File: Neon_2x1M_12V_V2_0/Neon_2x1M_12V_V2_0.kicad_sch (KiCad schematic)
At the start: 38 parts, among them J1 Conn_01x16_Pin, J2 Barrel_Jack_MountingPin, J3 Conn_01x16_Pin, J4 Barrel_Jack_MountingPin, J5 Barrel_Jack_MountingPin, J6 Conn_01x03_Pin, Q1 IRLML2502TRPBF, Q2 IRLML2502TRPBF, SW1 SW_Push, SW2 SW_Push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

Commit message: updated schematic and layout for V2.0
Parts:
- added J7, J8: Screw_Terminal_01x02, Connector_JST:JST_NV_B02P-NV_1x02_P5.00mm_Vertical, symbol Connector:Screw_Terminal_01x02
- J4, J5: now not fitted; now left out of the parts list
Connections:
- net +12V: now also J7.2 (Pin_2), J8.2 (Pin_2)
- net B_Jack: now also J8.1 (Pin_1); no longer J4.2
- net P_Jack: now also J4.2, J7.1 (Pin_1)
- net BUCK_SW: now reaches D2.1 (K), L1.1, U3.2 (OUT)

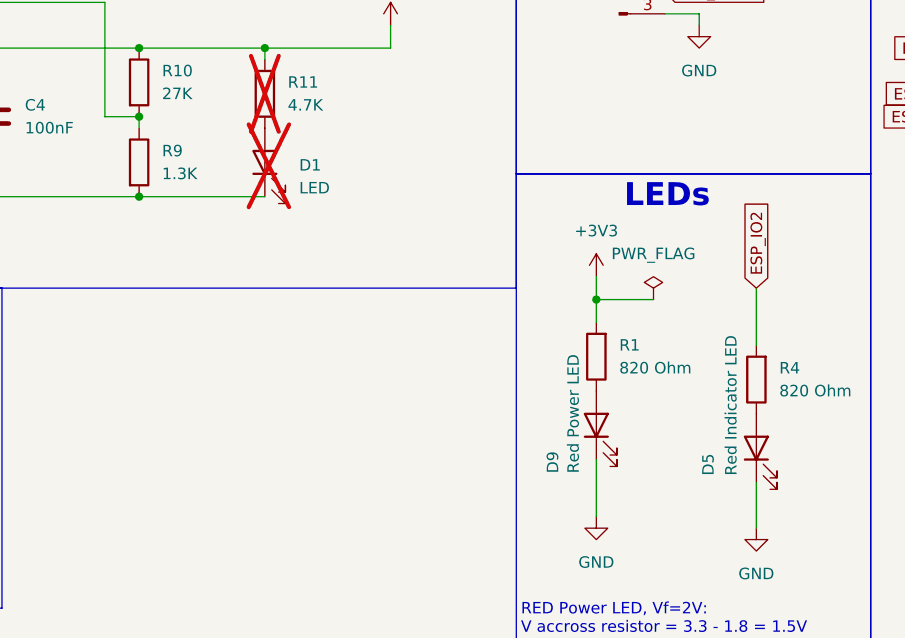
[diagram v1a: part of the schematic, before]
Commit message: updated BOM and generated BOM csv file also updated schematic and layout along
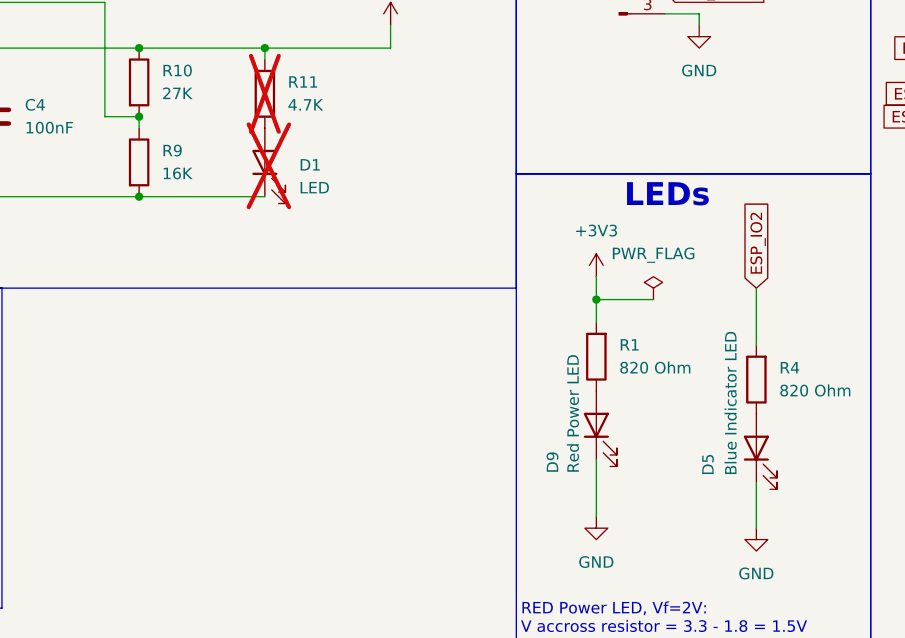
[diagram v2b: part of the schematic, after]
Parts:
- D5: value Red Indicator LED -> Blue Indicator LED
- R3, R6, R7, R8: footprint Resistor_SMD:R_0805_2012Metric_Pad1.20x1.40mm_HandSolder -> Resistor_SMD:R_1210_3225Metric_Pad1.30x2.65mm_HandSolder; link https://uge-one.com/product/0805-smd-chip-resistor-10k/?srs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 -> https://makerselectronics.com/product/chip-resistor-smd-10k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
- R9: value 1.3K -> 16K
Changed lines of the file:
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@@
 			)
 		)
-		(property "Footprint" "Resistor_SMD:R_0805_2012Metric_Pad1.20x1.40mm_HandSolder"
+		(property "Footprint" "Resistor_SMD:R_1210_3225Metric_Pad1.30x2.65mm_HandSolder"
 			(at 212.598 132.08 90)
 			(hide yes)
@@
 			)
 		)
-		(property "link" "https://uge-one.com/product/0805-smd-chip-resistor-10k/?srsltid=AfmBOorGllG0mYHf8TnX2S13KIvxT3n0IIoJoriv-BR9zB-dGtGjm2Vg"
+		(property "link" "https://makerselectronics.com/product/chip-resistor-smd-10k%cf%89-%c2%b15-0-5w-%c2%b1100ppm-%e2%84%83-1210/"
 			(at 210.82 132.08 0)
 			(hide yes)
@@
 			)
 		)
-		(property "Footprint" "Resistor_SMD:R_0805_2012Metric_Pad1.20x1.40mm_HandSolder"
+		(property "Footprint" "Resistor_SMD:R_1210_3225Metric_Pad1.30x2.65mm_HandSolder"
 			(at 198.628 132.08 90)
 			(hide yes)
@@
 			)
 		)
-		(property "link" "https://uge-one.com/product/0805-smd-chip-resistor-10k/?srsltid=AfmBOorGllG0mYHf8TnX2S13KIvxT3n0IIoJoriv-BR9zB-dGtGjm2Vg"
+		(property "link" "https://makerselectronics.com/product/chip-resistor-smd-10k%cf%89-%c2%b15-0-5w-%c2%b1100ppm-%e2%84%83-1210/"
 			(at 196.85 132.08 0)
 			(hide yes)
@@
 			)
 		)
-		(property "Footprint" "Resistor_SMD:R_0805_2012Metric_Pad1.20x1.40mm_HandSolder"
+		(property "Footprint" "Resistor_SMD:R_1210_3225Metric_Pad1.30x2.65mm_HandSolder"
 			(at 35.052 129.54 90)
 			(hide yes)
@@
 			)
 		)
-		(property "link" "https://uge-one.com/product/0805-smd-chip-resistor-10k/?srsltid=AfmBOorGllG0mYHf8TnX2S13KIvxT3n0IIoJoriv-BR9zB-dGtGjm2Vg"
+		(property "link" "https://makerselectronics.com/product/chip-resistor-smd-10k%cf%89-%c2%b15-0-5w-%c2%b1100ppm-%e2%84%83-1210/"
 			(at 36.83 129.54 0)
 			(hide yes)
@@
 			)
 		)
-		(property "Footprint" "Resistor_SMD:R_0805_2012Metric_Pad1.20x1.40mm_HandSolder"
+		(property "Footprint" "Resistor_SMD:R_1210_3225Metric_Pad1.30x2.65mm_HandSolder"
 			(at 35.052 161.29 90)
 			(hide yes)
@@
 			)
 		)
-		(property "link" "https://uge-one.com/product/0805-smd-chip-resistor-10k/?srsltid=AfmBOorGllG0mYHf8TnX2S13KIvxT3n0IIoJoriv-BR9zB-dGtGjm2Vg"
+		(property "link" "https://makerselectronics.com/product/chip-resistor-smd-10k%cf%89-%c2%b15-0-5w-%c2%b1100ppm-%e2%84%83-1210/"
 			(at 36.83 161.29 0)
 			(hide yes)
@@
 			)
 		)
-		(property "Value" "1.3K"
+		(property "Value" "16K"
 			(at 144.78 50.7999 0)
 			(show_name no)
@@
 			)
 		)
-		(property "Value" "Red Indicator LED"
+		(property "Value" "Blue Indicator LED"
 			(at 208.026 84.328 0)
 			(show_name no)
